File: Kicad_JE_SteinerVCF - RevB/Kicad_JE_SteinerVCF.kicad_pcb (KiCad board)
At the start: 2 copper layers, 100 x 100 mm, 154 parts, among them J101 HP, J102 BP, J103 LP, J104 Out, J105 CV, J201 HP, J202 BP, J203 LP, J204 Out, J205 CV, J301 Sine, J302 Triangle, J303 Square, J304 CV Vactrol, J305 CV, P101 Doepfer_Power_10pin, P201 Doepfer_Power_10pin, P301 Doepfer_Power_10pin, Q101 BC559, Q102 BC549, Q103 BC549, Q104 BC549, Q201 MMBT2907A, Q202 MMBT2222A, Q203 MMBT2222A, Q204 MMBT2222A, U301 TL074, U302 ICL8038

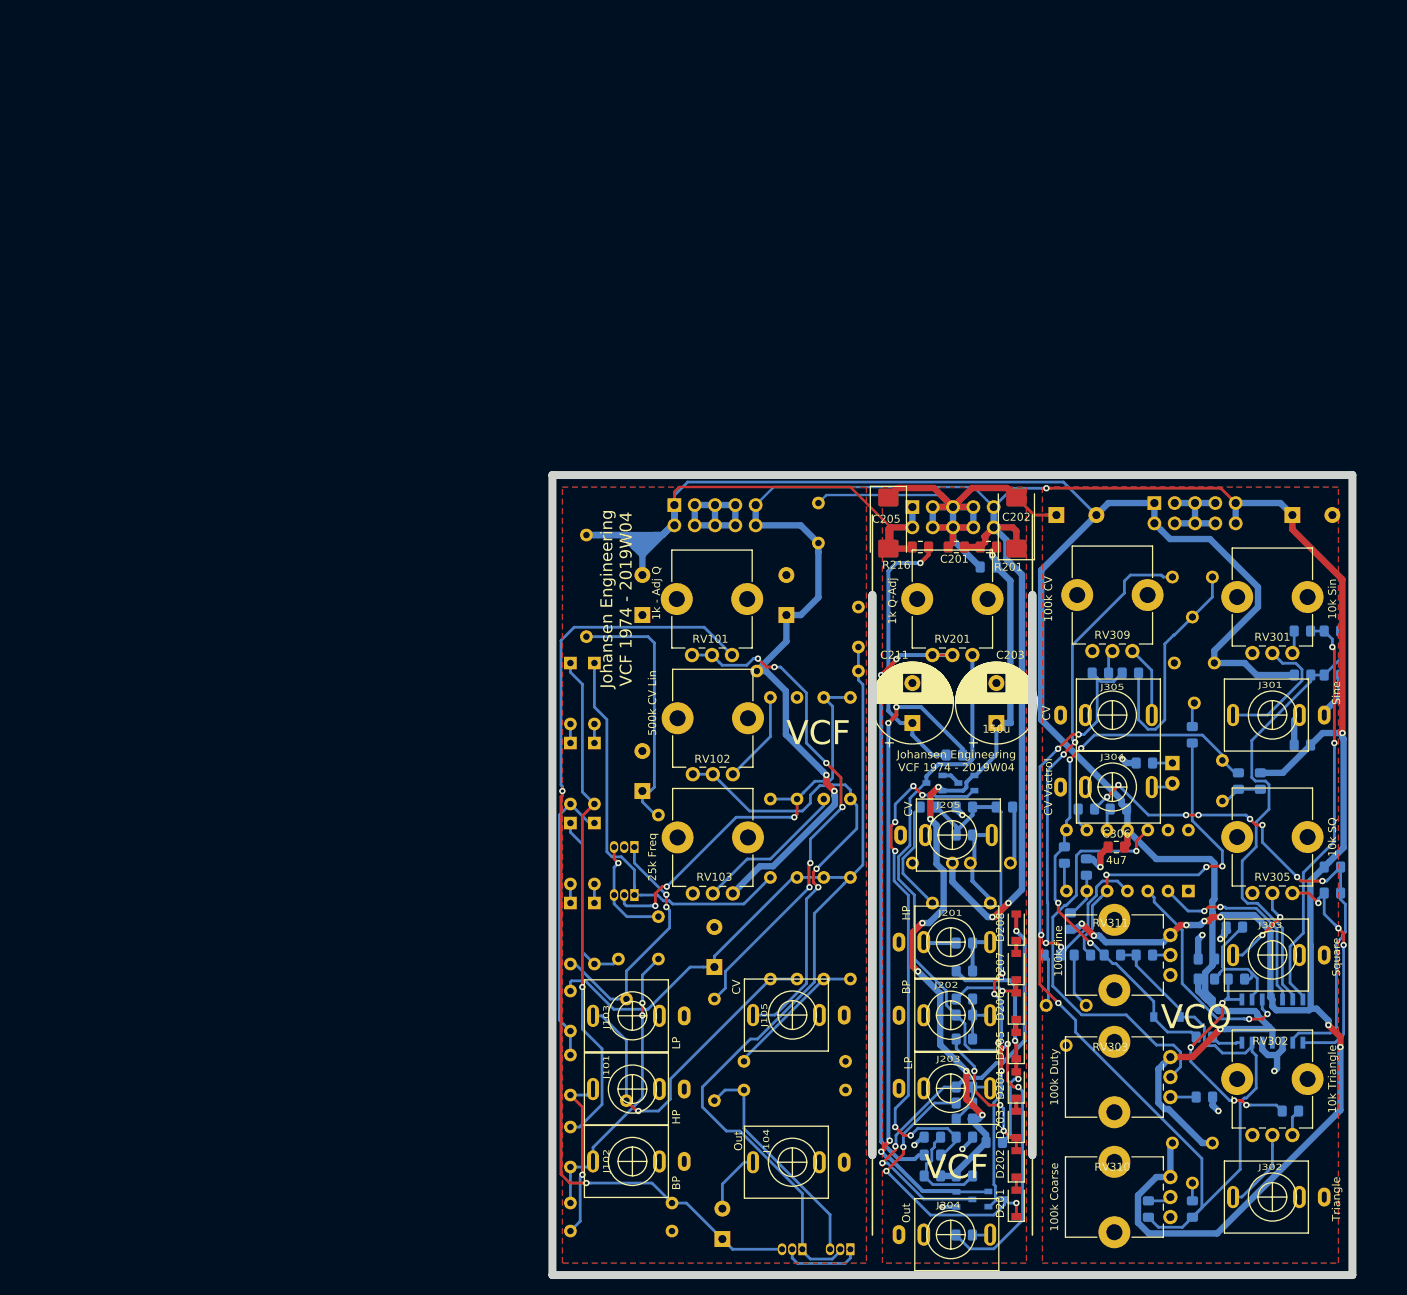
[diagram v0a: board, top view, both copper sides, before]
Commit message: VCF SMD routed
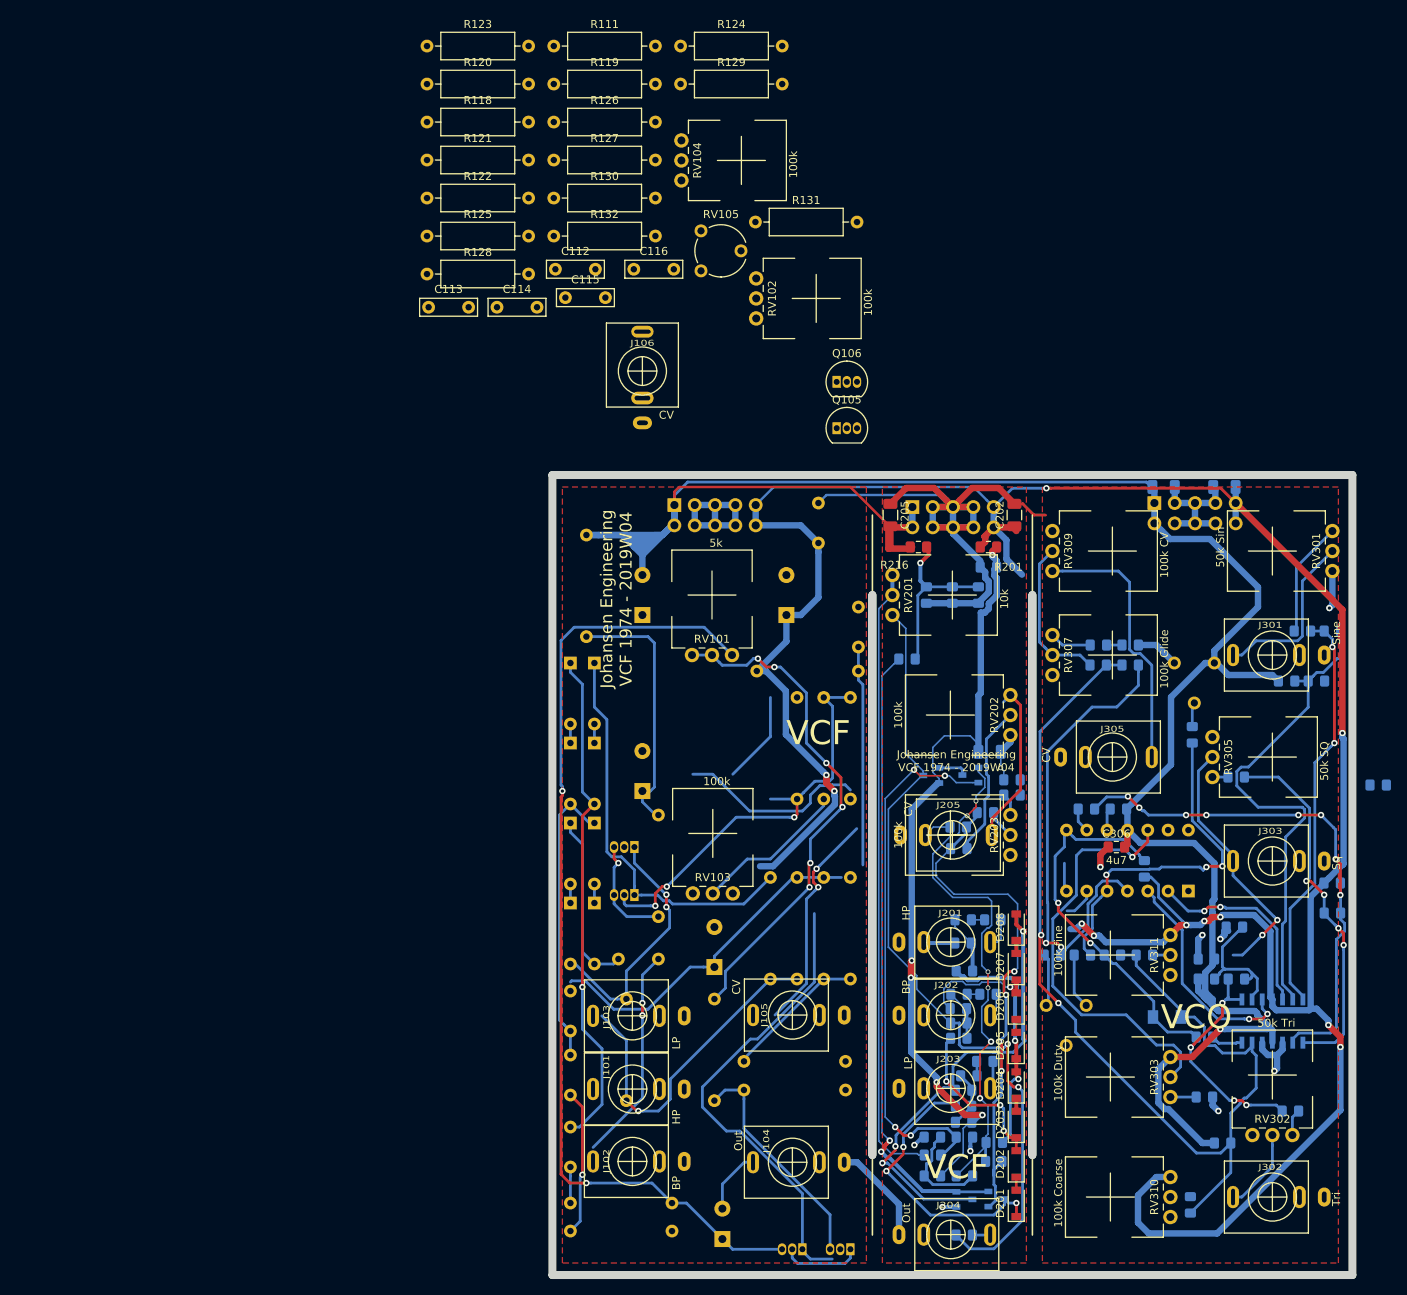
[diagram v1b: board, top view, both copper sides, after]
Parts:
- removed J304: CV Vactrol, AJ-Dropbox-Kicad:PJ301SM
- removed LED301: LED, LED_THT:LED_D5.0mm
- removed R318: 0R, Resistor_SMD:R_0805_2012Metric_Pad1.15x1.40mm_HandSolder
- removed R319: LDR03, OptoDevice:R_LDR_7x6mm_P5.1mm_Vertical
- removed R321, R324: 470k, Resistor_SMD:R_0805_2012Metric_Pad1.15x1.40mm_HandSolder
- removed RV202 1V/Oct: 500k, Potentiometer_THT:Potentiometer_Piher_PT-6-V_Vertical
- removed RV203 Freq: 25k, Potentiometer_THT:Potentiometer_Piher_PT-6-V_Vertical
- removed RV308: 100k min trim, Potentiometer_THT:Potentiometer_Piher_PT-6-V_Vertical
- added C112: 100n, Capacitor_THT:C_Rect_L7.0mm_W2.0mm_P5.00mm, F.Cu at (50.4, 24.3)
- added C113: 10u, Capacitor_THT:C_Rect_L7.0mm_W2.0mm_P5.00mm, F.Cu at (34.5, 29.0)
- added C114: 220n, Capacitor_THT:C_Rect_L7.0mm_W2.0mm_P5.00mm, F.Cu at (43.1, 29.0)
- added C115: 220n, Capacitor_THT:C_Rect_L7.0mm_W2.0mm_P5.00mm, F.Cu at (51.6, 27.8)
- added C116: 10u, Capacitor_THT:C_Rect_L7.0mm_W2.0mm_P5.00mm, F.Cu at (60.2, 24.3)
- added C212: 220n, Capacitor_SMD:C_0805_2012Metric_Pad1.15x1.40mm_HandSolder, B.Cu at (101.3, 105.6)
- added C213: 470n, Capacitor_SMD:C_0805_2012Metric_Pad1.15x1.40mm_HandSolder, B.Cu at (100.8, 114.9)
- added C214: 1u, Capacitor_SMD:C_0805_2012Metric_Pad1.15x1.40mm_HandSolder, B.Cu at (102.0, 125.1)
- added C215: 22u, Capacitor_SMD:C_0805_2012Metric_Pad1.15x1.40mm_HandSolder, B.Cu at (100.0, 65.0)
- added C216: 22u, Capacitor_SMD:C_0805_2012Metric_Pad1.15x1.40mm_HandSolder, B.Cu at (96.8, 65.0)
- added C308: 1u, Capacitor_SMD:C_0805_2012Metric_Pad1.15x1.40mm_HandSolder, B.Cu at (122.2, 71.2)
- added J106: CV, AJ-Dropbox-Kicad:PJ301SM, F.Cu at (61.2, 37.0)
- added Q105: BC549, Package_TO_SOT_THT:TO-92_Inline, F.Cu at (85.5, 44.1)
- added Q106: BC549, Package_TO_SOT_THT:TO-92_Inline, F.Cu at (85.5, 38.4)
- added R118: 100k, Resistor_THT:R_Axial_DIN0309_L9.0mm_D3.2mm_P12.70mm_Horizontal, F.Cu at (34.3, 5.88)
- added R119: 1k, Resistor_THT:R_Axial_DIN0309_L9.0mm_D3.2mm_P12.70mm_Horizontal, F.Cu at (50.2, 1.13)
- added R120: 47k, Resistor_THT:R_Axial_DIN0309_L9.0mm_D3.2mm_P12.70mm_Horizontal, F.Cu at (34.3, 1.13)
- added R121: 10k, Resistor_THT:R_Axial_DIN0309_L9.0mm_D3.2mm_P12.70mm_Horizontal, F.Cu at (34.3, 10.6)
- added R122: 1k, Resistor_THT:R_Axial_DIN0309_L9.0mm_D3.2mm_P12.70mm_Horizontal, F.Cu at (34.3, 15.4)
- added R123: 47k, Resistor_THT:R_Axial_DIN0309_L9.0mm_D3.2mm_P12.70mm_Horizontal, F.Cu at (34.3, -3.62)
- added R124: 220k, Resistor_THT:R_Axial_DIN0309_L9.0mm_D3.2mm_P12.70mm_Horizontal, F.Cu at (66.0, -3.62)
- added R125: 10k, Resistor_THT:R_Axial_DIN0309_L9.0mm_D3.2mm_P12.70mm_Horizontal, F.Cu at (34.3, 20.1)
- added R126: 1k, Resistor_THT:R_Axial_DIN0309_L9.0mm_D3.2mm_P12.70mm_Horizontal, F.Cu at (50.2, 5.88)
- added R127: 82k, Resistor_THT:R_Axial_DIN0309_L9.0mm_D3.2mm_P12.70mm_Horizontal, F.Cu at (50.2, 10.6)
- added R128: 47k, Resistor_THT:R_Axial_DIN0309_L9.0mm_D3.2mm_P12.70mm_Horizontal, F.Cu at (34.3, 24.9)
- added R129: 15k, Resistor_THT:R_Axial_DIN0309_L9.0mm_D3.2mm_P12.70mm_Horizontal, F.Cu at (66.0, 1.13)
- added R130: 1k, Resistor_THT:R_Axial_DIN0309_L9.0mm_D3.2mm_P12.70mm_Horizontal, F.Cu at (50.2, 15.4)
- added R131: 47k, Resistor_THT:R_Axial_DIN0309_L9.0mm_D3.2mm_P12.70mm_Horizontal, F.Cu at (75.4, 18.4)
- added R132: 10k, Resistor_THT:R_Axial_DIN0309_L9.0mm_D3.2mm_P12.70mm_Horizontal, F.Cu at (50.2, 20.1)
- added R218: 47k, Resistor_SMD:R_0805_2012Metric_Pad1.15x1.40mm_HandSolder, B.Cu at (105.0, 105.6)
- added R219: 47k, Resistor_SMD:R_0805_2012Metric_Pad1.15x1.40mm_HandSolder, B.Cu at (104.5, 114.9)
- added R220: 47k, Resistor_SMD:R_0805_2012Metric_Pad1.15x1.40mm_HandSolder, B.Cu at (104.0, 123.3)
- added R221: 12k, Resistor_SMD:R_0805_2012Metric_Pad1.15x1.40mm_HandSolder, B.Cu at (107.5, 90.0)
- added RV104: 100k, AJ:Potentiometer_China_RK09_Single_Vertical_AJ, F.Cu at (66.1, 13.2)
- added RV105: 2k, Potentiometer_THT:Potentiometer_Piher_PT-6-V_Vertical, F.Cu at (68.6, 24.5)
- added RV202: 100k, AJ-Dropbox-Kicad:Potentiometer_China_RK09_Single_Vertical_AJ, F.Cu at (107.2, 77.5)
- added RV203: 100k, AJ-Dropbox-Kicad:Potentiometer_China_RK09_Single_Vertical_AJ, F.Cu at (107.2, 92.5)
- C103, C111: value 150u -> 100u
- C201: moved to B.Cu
- C202, C205: footprint Capacitor_Tantalum_SMD:CP_EIA-7343-15_Kemet-W_Pad2.25x2.55mm_HandSolder -> Capacitor_SMD:C_1206_3216Metric
- C203: footprint Capacitor_THT:CP_Radial_D10.0mm_P5.00mm -> Capacitor_SMD:C_1206_3216Metric; moved to B.Cu
- C211: value 150u -> 100u; footprint Capacitor_THT:CP_Radial_D10.0mm_P5.00mm -> Capacitor_SMD:C_0805_2012Metric_Pad1.15x1.40mm_HandSolder; moved to B.Cu
- C302, C304: footprint Capacitor_THT:CP_Radial_D10.0mm_P5.00mm -> Capacitor_SMD:C_1206_3216Metric
- D302: footprint Diode_SMD:D_SOD-123 -> Diode_SMD:D_MiniMELF
- J302: value Triangle -> Tri
- J303: value Square -> Sq
- R104: value 18k -> 15k
- R111: value 220k -> 10k; moved to F.Cu
- R117: value 1k -> 680
- R204: value 18k -> 12k
- R211: value 220k -> 82k
- R307, R308, R315: value 0R -> 680R
- R317: value 0R -> 100r
- R320: value 470k -> 220k
- R328: value 0R -> 10R
- RV101: value 1k - Adj Q -> 5k; footprint Potentiometer_THT:Potentiometer_Alps_RK09K_Single_Vertical -> AJ:Potentiometer_China_RK09_Single_Vertical_AJ
- RV102: value 500k CV Lin -> 100k; footprint Potentiometer_THT:Potentiometer_Alps_RK09K_Single_Vertical -> AJ:Potentiometer_China_RK09_Single_Vertical_AJ
- RV103: value 25k Freq -> 100k; footprint Potentiometer_THT:Potentiometer_Alps_RK09K_Single_Vertical -> AJ:Potentiometer_China_RK09_Single_Vertical_AJ
- RV201: value 1k Q-Adj -> 10k; footprint Potentiometer_THT:Potentiometer_Alps_RK09K_Single_Vertical -> AJ:Potentiometer_China_RK09_Single_Vertical_AJ
- RV301: value 10k Sin -> 50k Sin; footprint Potentiometer_THT:Potentiometer_Alps_RK09K_Single_Vertical -> AJ:Potentiometer_China_RK09_Single_Vertical_AJ
- RV302: value 10k Triangle -> 50k Tri; footprint Potentiometer_THT:Potentiometer_Alps_RK09K_Single_Vertical -> AJ:Potentiometer_China_RK09_Single_Vertical_AJ
- RV303, RV309, RV310, RV311: footprint Potentiometer_THT:Potentiometer_Alps_RK09K_Single_Vertical -> AJ:Potentiometer_China_RK09_Single_Vertical_AJ
- RV304: value 1k Symetry -> 1k
- RV305: value 10k SQ -> 50k SQ; footprint Potentiometer_THT:Potentiometer_Alps_RK09K_Single_Vertical -> AJ:Potentiometer_China_RK09_Single_Vertical_AJ
- RV306: value 100k LF Sym -> 100k
- RV307: value 10k Max Trim -> 100k Glide; footprint Potentiometer_THT:Potentiometer_Piher_PT-6-V_Vertical -> AJ:Potentiometer_China_RK09_Single_Vertical_AJ; moved to F.Cu
- moved R111 97.9 mm to (50.2, -3.62), turned to 0 degrees
- moved RV102 57.1 mm to (75.5, 30.4), turned to 0 degrees
- moved R211 44.3 mm to (105.2, 135.8)
- moved C201 29.9 mm to (107.5, 88.1)
- moved R317 27.8 mm to (118.2, 71.2), turned to 0 degrees
- moved R315 27.5 mm to (135.5, 87.8), turned to 0 degrees
- moved RV307 23.5 mm to (112.5, 75.0), turned to 0 degrees
- moved C211 18.0 mm to (103.2, 65.0)
- moved RV305 17.6 mm to (132.5, 87.8), turned to 0 degrees
- moved R320 16.1 mm to (124.0, 99.2)
- moved RV301 16.0 mm to (147.5, 57.0), turned to 180 degrees
- moved RV309 14.1 mm to (112.5, 62.0), turned to 0 degrees
- moved C304 13.8 mm to (126.4, 51.5), turned to 180 degrees
- moved R214 13.4 mm to (94.3, 73.0), turned to 180 degrees
- moved J303 11.8 mm to (140.0, 98.2)
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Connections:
- C106 pad 1: +10V -> Net-(C106-Pad1)
- C206 pad 1: VCC -> Net-(C206-Pad1)
- C211 pad 1: Net-(C211-Pad1) -> GNDA
- C211 pad 2: GNDA -> Net-(C211-Pad2)
- J101 pad T: HP -> Net-(J101-PadT)
- J102 pad T: BP -> Net-(J102-PadT)
- J103 pad T: LP -> Net-(J103-PadT)
- J105 pad T: CV -> CV2
- J201 pad T: HP2 -> Net-(J201-PadT)
- J202 pad T: BP2 -> Net-(J202-PadT)
- J203 pad T: LP2 -> Net-(J203-PadT)
- J205 pad T: CV2 -> CV2.1
- J301 pad TN: GNDA -> (no net)
- J302 pad TN: GNDA -> (no net)
- J303 pad TN: GNDA -> (no net)
- Q102 pad 2: +10V -> Net-(C106-Pad1)
- Q103 pad 2: Net-(Q103-Pad2) -> CV
- Q202 pad 1: VCC -> Net-(C206-Pad1)
- Q203 pad 1: Net-(Q203-Pad1) -> CV2.0
- R103 pad 2: +10V -> Net-(C106-Pad1)
- R111 pad 1: Net-(Q103-Pad2) -> Net-(Q105-Pad1)
- R111 pad 2: Net-(R111-Pad2) -> +12VA
- R112 pad 1: Net-(Q103-Pad2) -> CV
- R112 pad 2: CV -> Net-(R112-Pad2)
- R115 pad 1: Net-(Q103-Pad2) -> CV
- R117 pad 1: GNDA -> Net-(R117-Pad1)
- R117 pad 2: Net-(Q103-Pad2) -> CV
- R203 pad 2: VCC -> Net-(C206-Pad1)
- R211 pad 1: Net-(Q203-Pad1) -> Net-(C206-Pad1)
- R211 pad 2: Net-(R211-Pad2) -> CV2.0
- R212 pad 1: Net-(Q203-Pad1) -> CV2.0
- R212 pad 2: CV2 -> Net-(R212-Pad2)
- R214 pad 1: Net-(C211-Pad1) -> Net-(C211-Pad2)
- R215 pad 1: Net-(Q203-Pad1) -> CV2.0
- R216 pad 2: Net-(C211-Pad1) -> Net-(C211-Pad2)
- R217 pad 2: Net-(Q203-Pad1) -> CV2.0
- R315 pad 2: +12VA -> Net-(R311-Pad1)
- R317 pad 1: Net-(R315-Pad1) -> Net-(R317-Pad1)
- R317 pad 2: GNDA -> Net-(C308-Pad2)
- R320 pad 1: Net-(R319-Pad1) -> +12VA
- R322 pad 1: Net-(R322-Pad1) -> Net-(R312-Pad1)
- R323 pad 1: Net-(R323-Pad1) -> Net-(C307-Pad2)
- R323 pad 2: Net-(C307-Pad2) -> -12VA
- RV102 pad 1: Net-(R111-Pad2) -> CV2
- RV102 pad 2: CV -> Net-(R131-Pad2)
- RV102 pad 3: CV -> GNDA
- RV103 pad 1: +12VA -> Net-(R132-Pad1)
- RV305 pad 1: Net-(R311-Pad1) -> Net-(R315-Pad1)
- RV307 pad 1: Net-(R322-Pad1) -> Net-(R325-Pad2)
- RV307 pad 2: Net-(R322-Pad1) -> Net-(R325-Pad2)
- RV307 pad 3: Net-(R312-Pad1) -> Net-(R317-Pad1)
- U302 pad 6: Net-(R315-Pad1) -> GNDA
- U302 pad 7: Net-(R318-Pad2) -> (no net)
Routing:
- net +12VA: track 399.3 -> 329.3 mm, vias 13 -> 11
- net Net-(C206-Pad1): track 0.00 -> 67.0 mm, vias 0 -> 6
- net CV2.0: track 0.00 -> 64.3 mm, vias 0 -> 4
- net Net-(Q203-Pad1): track 64.1 -> 0.00 mm, vias 4 -> 0
- net Net-(C211-Pad1): track 53.9 -> 0.00 mm, vias 1 -> 0
- net Net-(Q103-Pad2): track 53.1 -> 0.00 mm, vias 3 -> 0
- net CV: track 59.8 -> 105.0 mm, vias 2 -> 5
- net GNDA: track 153.2 -> 185.6 mm
- net Net-(R322-Pad1): track 30.5 -> 0.00 mm
- net CV-VCO: track 9.00 -> 33.5 mm
- net Net-(C307-Pad1): track 69.5 -> 47.2 mm, vias 4 -> 2
- net Net-(C211-Pad2): track 0.00 -> 21.8 mm, vias 0 -> 1
- net CV2.1: track 0.00 -> 21.4 mm
- net Square: track 11.3 -> 32.5 mm
- net -12VA: track 319.9 -> 299.7 mm
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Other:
- board text added: "VC0 RevB 8083"
- board text removed: "VC0 8083"

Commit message: fiddleing w THT VCF
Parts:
- C102, C103, C105, C111: footprint Capacitor_THT:CP_Radial_D10.0mm_P5.00mm -> Capacitor_THT:C_Radial_D8.0mm_H7.0mm_P3.50mm
- C107: footprint Capacitor_THT:CP_Radial_D10.0mm_P3.80mm -> Capacitor_THT:C_Radial_D8.0mm_H7.0mm_P3.50mm
- C112, C114, C115, Q105, Q106, R111, R118, R119, R120, R121, R122, R124, R125, R126, R128, R129, R130, R132: moved to B.Cu
- C113, C116: footprint Capacitor_THT:C_Rect_L7.0mm_W2.0mm_P5.00mm -> Capacitor_THT:C_Radial_D8.0mm_H7.0mm_P3.50mm; moved to B.Cu
- moved R123 151.7 mm to (52.2, 147.0), turned to 90 degrees
- moved R129 146.8 mm to (25.6, 142.3)
- moved R119 138.7 mm to (-1.12, 130.0)
- moved C116 115.1 mm to (26.2, 134.3)
- moved R130 113.1 mm to (22.2, 125.0)
- moved C114 112.8 mm to (56.8, 141.0)
- moved R126 110.8 mm to (23.8, 113.5)
- moved R124 109.7 mm to (-16.2, 69.0)
- moved Q106 105.6 mm to (36.5, 131.8)
- moved J106 91.6 mm to (80.0, 126.7), turned to 90 degrees
- moved R127 87.8 mm to (70.2, 96.1), turned to 270 degrees
- moved C115 86.3 mm to (-14.8, 83.0)
- moved R132 78.5 mm to (-16.2, 62.0)
- moved R111 76.3 mm to (11.2, 62.0), turned to 180 degrees
- moved R131 75.3 mm to (70.2, 93.5), turned to 90 degrees
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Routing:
- net Net-(R104-Pad1): track 63.8 -> 0.00 mm, vias 6 -> 0
- net CV: track 105.0 -> 47.1 mm, vias 5 -> 2
- net +12VA: track 329.3 -> 308.0 mm, vias 11 -> 9
- net Net-(R115-Pad2): track 19.2 -> 0.00 mm
- net -12VA: track 299.7 -> 281.9 mm
- net Net-(C114-Pad2): track 0.00 -> 17.1 mm
- net BP: track 31.4 -> 47.1 mm
- net Net-(R111-Pad2): track 11.5 -> 0.00 mm
- net HP: track 18.2 -> 26.0 mm
- net Net-(R117-Pad1): track 0.00 -> 5.37 mm
- net Net-(J102-PadT): track 0.00 -> 3.45 mm
- net Net-(Q102-Pad3): track 28.6 -> 25.2 mm
- net LP: track 42.0 -> 44.2 mm
- net Net-(C107-Pad1): track 121.9 -> 124.0 mm
- net Out: track 7.83 -> 8.92 mm
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
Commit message: VCF THT Placed
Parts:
- C113, Q105, R101, R111, R112, R115, R117, R118, R119, R121, R122, R132: moved to F.Cu
- R127, RV105: moved to B.Cu
- moved R132 102.2 mm to (83.5, 84.0), turned to 270 degrees
- moved R125 90.2 mm to (70.8, 89.2)
- moved Q105 87.9 mm to (87.5, 112.0), turned to 90 degrees
- moved C113 85.3 mm to (86.0, 122.2), turned to 90 degrees
- moved R111 85.0 mm to (77.5, 115.2), turned to 270 degrees
- moved R122 83.2 mm to (81.0, 128.0), turned to 90 degrees
- moved R121 80.6 mm to (71.5, 122.8), turned to 90 degrees
- moved R124 76.2 mm to (54.5, 97.2)
- moved R129 76.2 mm to (83.5, 92.8), turned to 180 degrees
- moved C116 73.8 mm to (77.8, 81.5), turned to 180 degrees
- moved R119 70.4 mm to (69.2, 128.0), turned to 270 degrees
- moved C115 68.1 mm to (52.2, 95.2), turned to 270 degrees
- moved R118 67.8 mm to (75.0, 110.0), turned to 270 degrees
- moved C112 64.0 mm to (62.2, 111.8), turned to 180 degrees
- moved J106 63.2 mm to (80.0, 63.5)
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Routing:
- net +10V: track 130.0 -> 0.00 mm
- net Net-(C107-Pad1): track 124.0 -> 0.00 mm, vias 2 -> 0
- net Net-(C108-Pad1): track 63.2 -> 0.00 mm, vias 1 -> 0
- net Net-(D101-Pad1): track 50.5 -> 0.00 mm
- net CV: track 47.1 -> 0.00 mm, vias 2 -> 0
- net BP: track 47.1 -> 0.00 mm, vias 2 -> 0
- net LP: track 44.2 -> 0.00 mm, vias 1 -> 0
- net FilterOut: track 36.5 -> 0.00 mm
- net Net-(C111-Pad1): track 33.1 -> 0.00 mm
- net Net-(D108-Pad2): track 31.9 -> 0.00 mm, vias 2 -> 0
- net HP: track 26.0 -> 0.00 mm, vias 1 -> 0
- net Net-(Q102-Pad3): track 25.2 -> 0.00 mm
- net Net-(C110-Pad1): track 22.1 -> 0.00 mm
- net Net-(R102-Pad1): track 18.5 -> 0.00 mm
- net Net-(C114-Pad2): track 17.1 -> 0.00 mm
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
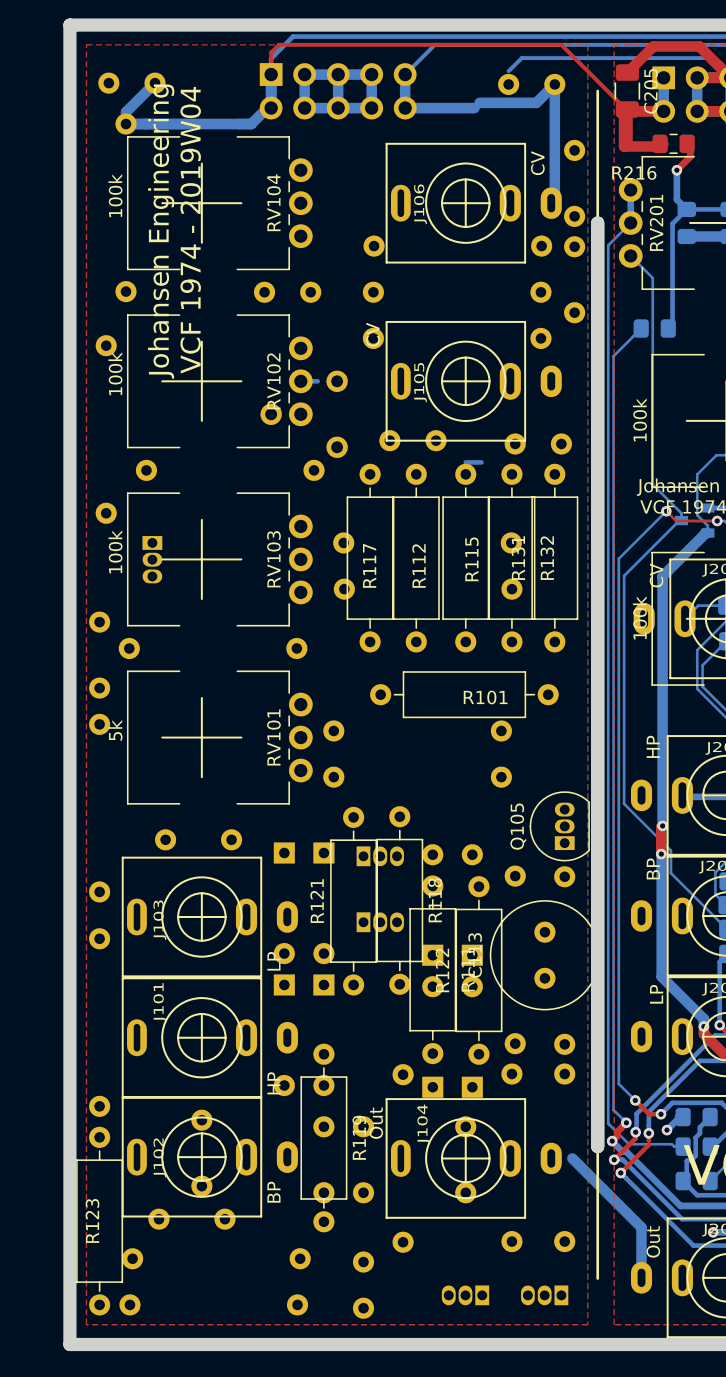
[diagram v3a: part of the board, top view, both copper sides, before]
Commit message: Routed THT
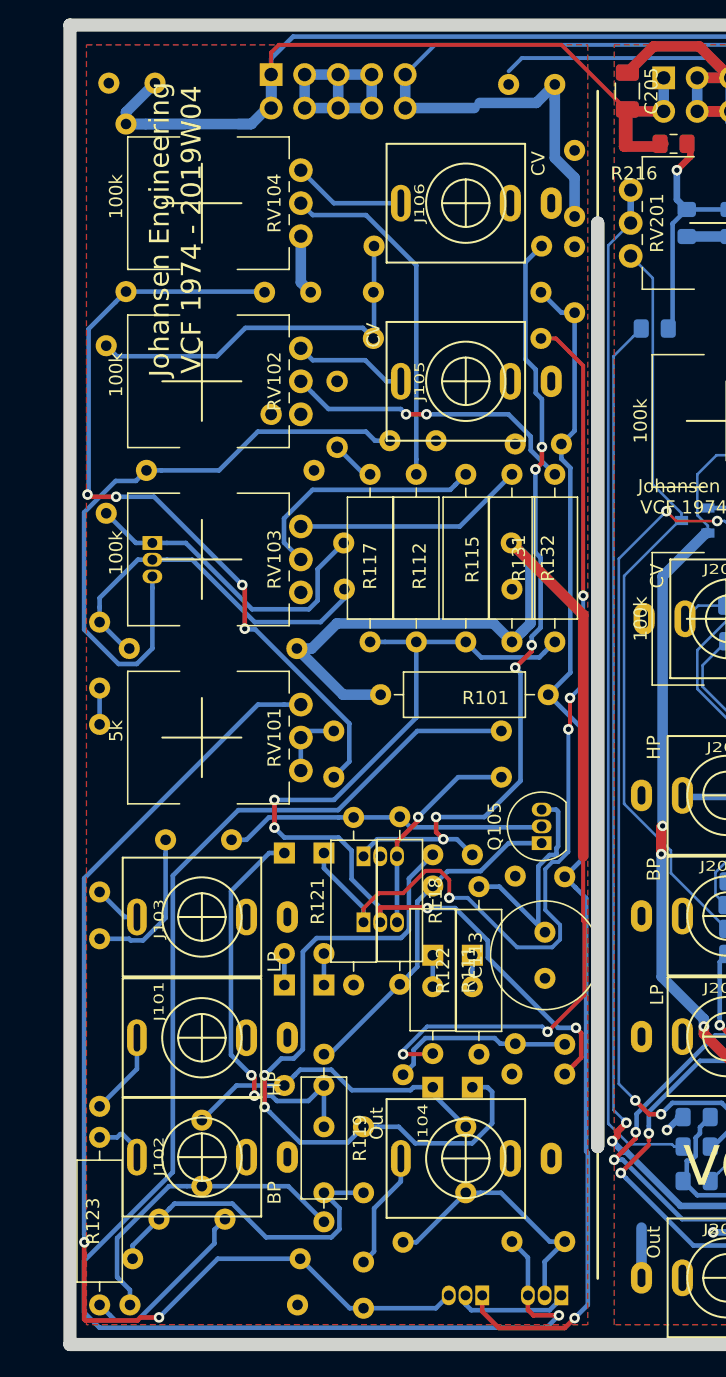
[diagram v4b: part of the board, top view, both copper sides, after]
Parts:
- moved Q105 1.75 mm to (85.8, 112.0)
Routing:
- net Net-(Q102-Pad3): track 0.00 -> 110.4 mm, vias 0 -> 1
- net +10V: track 0.00 -> 92.5 mm, vias 0 -> 1
- net +12VA: track 298.0 -> 389.2 mm, vias 7 -> 9
- net Net-(C107-Pad1): track 0.00 -> 86.9 mm, vias 0 -> 2
- net Net-(D101-Pad1): track 0.00 -> 76.5 mm, vias 0 -> 4
- net CV: track 0.00 -> 73.7 mm, vias 0 -> 4
- net Net-(D108-Pad2): track 0.00 -> 61.8 mm, vias 0 -> 6
- net Net-(C111-Pad1): track 0.00 -> 60.5 mm, vias 0 -> 4
- net Net-(C110-Pad1): track 0.00 -> 52.7 mm, vias 0 -> 2
- net Net-(C116-Pad2): track 0.00 -> 47.1 mm
- net Net-(C108-Pad1): track 0.00 -> 30.5 mm, vias 0 -> 2
- net LP: track 0.00 -> 28.8 mm
- net Net-(C115-Pad1): track 0.00 -> 28.1 mm
- net Net-(R112-Pad2): track 0.00 -> 26.5 mm
- net Net-(Q105-Pad1): track 0.00 -> 26.0 mm
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
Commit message: Labels
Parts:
- C301: moved to F.Cu
- moved C301 8.66 mm to (147.5, 95.2)
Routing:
- net +12VA: track 389.2 -> 434.8 mm, vias 9 -> 14
- net GNDA: track 179.3 -> 180.3 mm
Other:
- board text added: "Johansen Engineering VCF 1974 - 2019/10/05"
- board text added: "Johansen Engineering VCF 1974 - Rev B 2019/10/05"
- board text added: "Johansen Engineering VCO 8083 - 2019/10/05"
- board text removed: "Johansen Engineering VCF 1974 - 2019W04"
- board text removed: "Johansen Engineering VCO 8083 - 2019W04"
